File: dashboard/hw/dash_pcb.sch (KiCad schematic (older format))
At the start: 3 parts, among them J1 LCD, J2 DEBUG, U1 LPC11C24FBD48

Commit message: update connectors for the lcd actually used
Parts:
- added J3: LCD_BL, Connectors_JST:JST_XH_S03B-XH-A_03x2.50mm_Angled, symbol Conn_01x03
- added RV1: 10k, Potentiometers:Potentiometer_Trimmer_ACP_CA6v_Horizontal, symbol POT
- J1: footprint Socket_Strips:Socket_Strip_Straight_2x11_Pitch2.54mm -> Socket_Strips:Socket_Strip_Straight_2x10_Pitch2.54mm; symbol Conn_02x11_Odd_Even -> Conn_02x10_Odd_Even
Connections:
- wire segments 22 -> 25
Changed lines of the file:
@@
 $EndComp
 $Comp
-L Conn_02x11_Odd_Even J1
+L Conn_02x10_Odd_Even J1
 U 1 1 5ADCA11A
-P 9200 3300
-F 0 "J1" H 9250 3900 50  0000 C CNN
-F 1 "LCD" H 9250 2700 50  0000 C CNN
-F 2 "Socket_Strips:Socket_Strip_Straight_2x11_Pitch2.54mm" H 9200 3300 50  0001 C CNN
-F 3 "" H 9200 3300 50  0001 C CNN
-	1    9200 3300
-	1    0    0    -1
-$EndComp
-$Comp
-L GND #PWR7
+P 9200 3200
+F 0 "J1" H 9250 3700 50  0000 C CNN
+F 1 "LCD" H 9250 2600 50  0000 C CNN
+F 2 "Socket_Strips:Socket_Strip_Straight_2x10_Pitch2.54mm" H 9200 3200 50  0001 C CNN
+F 3 "" H 9200 3200 50  0001 C CNN
+	1    9200 3200
+	1    0    0    -1
+$EndComp
+$Comp
+L GND #PWR9
 U 1 1 5ADCA1A0
 P 9250 2600
-F 0 "#PWR7" H 9250 2350 50  0001 C CNN
+F 0 "#PWR9" H 9250 2350 50  0001 C CNN
 F 1 "GND" H 9250 2450 50  0000 C CNN
 F 2 "" H 9250 2600 50  0001 C CNN
@@
 Text Label 9000 3700 2    60   ~ 0
 LCD_FS
-Text Label 9500 3700 0    60   ~ 0
+Text Label 9000 3200 2    60   ~ 0
 LCD_VEE
-Text Label 9000 3800 2    60   ~ 0
-LCD_LED_A
-Text Label 9500 3800 0    60   ~ 0
-LCD_LED_K
 $Comp
 L GND #PWR2
@@
 Text Label 4400 3100 2    60   ~ 0
 LCD_DB1
-Text Label 4400 3200 2    60   ~ 0
+Text Label 4400 4800 2    60   ~ 0
 LCD_DB2
-Text Label 4400 3300 2    60   ~ 0
+Text Label 4400 4500 2    60   ~ 0
 LCD_DB3
 Text Label 4400 3400 2    60   ~ 0
@@
 $EndComp
 $Comp
-L +3V3 #PWR9
+L +3V3 #PWR11
 U 1 1 5ADCAB0C
 P 9500 5800
-F 0 "#PWR9" H 9500 5650 50  0001 C CNN
+F 0 "#PWR11" H 9500 5650 50  0001 C CNN
 F 1 "+3V3" H 9500 5940 50  0000 C CNN
 F 2 "" H 9500 5800 50  0001 C CNN
@@
 	9500 5800 9500 5900
 $Comp
-L GND #PWR8
+L GND #PWR10
 U 1 1 5ADCAB42
 P 9350 6300
-F 0 "#PWR8" H 9350 6050 50  0001 C CNN
+F 0 "#PWR10" H 9350 6050 50  0001 C CNN
 F 1 "GND" H 9350 6150 50  0000 C CNN
 F 2 "" H 9350 6300 50  0001 C CNN
@@
 Text Label 6800 2900 0    60   ~ 0
 LCD_C/~D
-Text Label 6800 3400 0    60   ~ 0
-LCD_~CE
 Text Label 6800 3300 0    60   ~ 0
 LCD_~RST
-Text Label 6800 4000 0    60   ~ 0
-LCD_FS
 Text Label 6800 3200 0    60   ~ 0
 LCD_~WR
@@
 CANL
 $Comp
-L +3V3 #PWR?
+L +3V3 #PWR8
 U 1 1 5AE5BC1B
 P 8800 2600
-F 0 "#PWR?" H 8800 2450 50  0001 C CNN
+F 0 "#PWR8" H 8800 2450 50  0001 C CNN
 F 1 "+3V3" H 8800 2740 50  0000 C CNN
 F 2 "" H 8800 2600 50  0001 C CNN
@@
 	1    0    0    -1
 $EndComp
+$Comp
+L +3V3 #PWR7
+U 1 1 5AE5BE05
+P 8450 3700
+F 0 "#PWR7" H 8450 3550 50  0001 C CNN
+F 1 "+3V3" H 8450 3840 50  0000 C CNN
+F 2 "" H 8450 3700 50  0001 C CNN
+F 3 "" H 8450 3700 50  0001 C CNN
+	1    8450 3700
+	1    0    0    -1
+$EndComp
+Wire Wire Line
+	8450 3700 9000 3700
+$Comp
+L GND #PWR6
+U 1 1 5AE5BE6A
+P 8450 3100
+F 0 "#PWR6" H 8450 2850 50  0001 C CNN
+F 1 "GND" H 8450 2950 50  0000 C CNN
+F 2 "" H 8450 3100 50  0001 C CNN
+F 3 "" H 8450 3100 50  0001 C CNN
+	1    8450 3100
+	1    0    0    -1
+$EndComp
+Wire Wire Line
+	8450 3100 9000 3100
+Text Label 10650 3500 2    60   ~ 0
+LCD_LED_A
+Text Label 10650 3700 2    60   ~ 0
+LCD_LED_K
+$Comp
+L Conn_01x03 J3
+U 1 1 5AE5C0EF
+P 10850 3600
+F 0 "J3" H 10850 3800 50  0000 C CNN
+F 1 "LCD_BL" H 10850 3400 50  0000 C CNN
+F 2 "Connectors_JST:JST_XH_S03B-XH-A_03x2.50mm_Angled" H 10850 3600 50  0001 C CNN
+F 3 "" H 10850 3600 50  0001 C CNN
+	1    10850 3600
+	1    0    0    -1
+$EndComp
+$Comp
+L POT RV1
+U 1 1 5AE5C369
+P 10550 2800
+F 0 "RV1" V 10375 2800 50  0000 C CNN
+F 1 "10k" V 10450 2800 50  0000 C CNN
+F 2 "Potentiometers:Potentiometer_Trimmer_ACP_CA6v_Horizontal" H 10550 2800 50  0001 C CNN
+F 3 "" H 10550 2800 50  0001 C CNN
+	1    10550 2800
+	0    -1   -1   0
+$EndComp
+$Comp
+L GND #PWR12
+U 1 1 5AE5C42C
+P 10850 2800
+F 0 "#PWR12" H 10850 2550 50  0001 C CNN
+F 1 "GND" H 10850 2650 50  0000 C CNN
+F 2 "" H 10850 2800 50  0001 C CNN
+F 3 "" H 10850 2800 50  0001 C CNN
+	1    10850 2800
+	1    0    0    -1
+$EndComp
+Wire Wire Line
+	10700 2800 10850 2800
+Text Label 10550 2650 0    60   ~ 0
+LCD_V0
+Text Label 10400 2800 2    60   ~ 0
+LCD_VEE
 $EndSCHEMATC

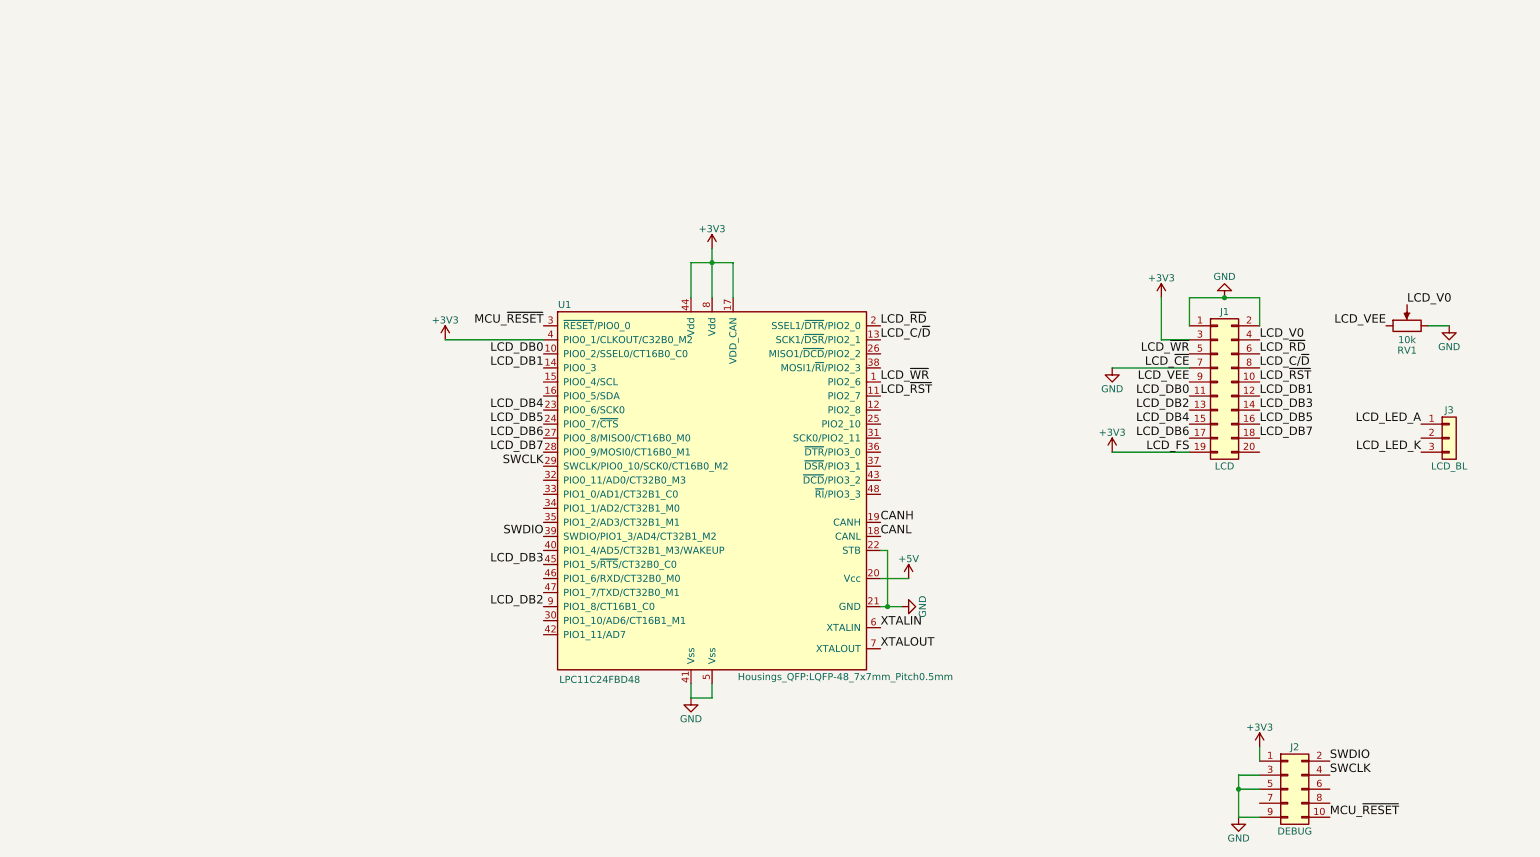
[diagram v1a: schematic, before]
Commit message: add misc passives to dash pcb
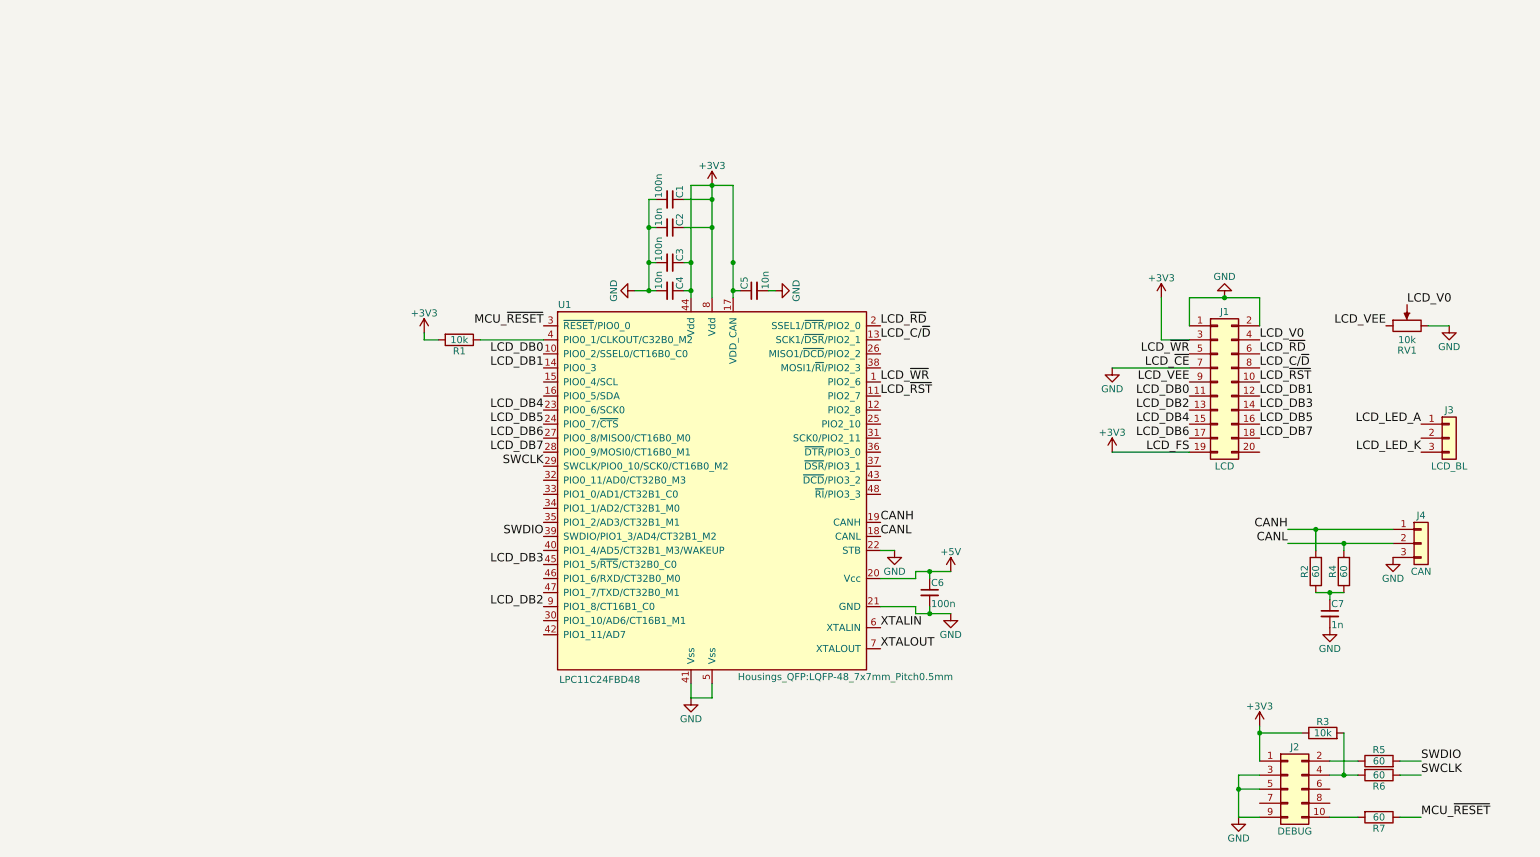
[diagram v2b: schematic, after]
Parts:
- added C1, C3, C6: 100n, Capacitors_SMD:C_0603, symbol C_Small
- added C2, C4, C5: 10n, Capacitors_SMD:C_0603, symbol C_Small
- added C7: 1n, Capacitors_SMD:C_0603, symbol C_Small
- added J4: CAN, Pin_Headers:Pin_Header_Angled_1x03_Pitch2.54mm, symbol Conn_01x03
- added R1, R3: 10k, Resistors_SMD:R_0603, symbol R
- added R2, R4, R5, R6, R7: 60, Resistors_SMD:R_0603, symbol R
- J2: footprint Pin_Headers:Pin_Header_Straight_2x05_Pitch1.27mm -> Pin_Headers:Pin_Header_Angled_2x05_Pitch1.27mm
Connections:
- net +3V3: now also C1.1, C2.1, C3.1, C4.1, C5.1, R1.2, R3.1; no longer U1.4 (PIO0_1/CLKOUT/C32B0_M2)
- net +5V: now also C6.1
- net CANH: now also J4.1 (Pin_1), R2.2
- net CANL: now also J4.2 (Pin_2), R4.2
- net GND: now also C1.2, C2.2, C3.2, C4.2, C5.2, C6.2, C7.2, J4.3 (Pin_3)
- net MCU_~RESET: now also R7.1; no longer J2.10 (Pin_10)
- net SWCLK: now also R6.1; no longer J2.4 (Pin_4)
- net SWDIO: now also R5.2; no longer J2.2 (Pin_2)
- new net: R1.1, U1.4 (PIO0_1/CLKOUT/C32B0_M2)
- new net: J2.10 (Pin_10), R7.2
- new net: J2.2 (Pin_2), R5.1
- new net: J2.4 (Pin_4), R3.2, R6.2
- new net: C7.1, R2.1, R4.1

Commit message: add schematic symbol for lmz21700 power module
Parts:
- added U?: LMZ21700, symbol LMZ21700
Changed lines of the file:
@@
 LIBS:valves
 LIBS:nxp_can
+LIBS:lmz21700
 LIBS:dash_pcb-cache
 EELAYER 25 0
@@
 Wire Wire Line
 	3550 2900 3650 2900
+$Comp
+L LMZ21700 U?
+U 1 1 5AEFF749
+P 1850 1450
+F 0 "U?" H 1600 850 60  0000 C CNN
+F 1 "LMZ21700" H 1850 1450 60  0000 C CNN
+F 2 "" H 2200 1300 60  0001 C CNN
+F 3 "" H 2200 1300 60  0001 C CNN
+	1    1850 1450
+	1    0    0    -1
+$EndComp
 $EndSCHEMATC

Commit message: add tps62175 which we are actually using
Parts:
- removed U?: LMZ21700, symbol LMZ21700
- added U?: TPS62175, symbol TPS62175
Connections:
- net labels added: 5VPG
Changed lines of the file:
@@
 LIBS:nxp_can
 LIBS:lmz21700
+LIBS:tps6217x
 LIBS:dash_pcb-cache
 EELAYER 25 0
@@
 Wire Wire Line
 	3550 2900 3650 2900
-$Comp
-L LMZ21700 U?
-U 1 1 5AEFF749
-P 1850 1450
-F 0 "U?" H 1600 850 60  0000 C CNN
-F 1 "LMZ21700" H 1850 1450 60  0000 C CNN
-F 2 "" H 2200 1300 60  0001 C CNN
-F 3 "" H 2200 1300 60  0001 C CNN
-	1    1850 1450
-	1    0    0    -1
-$EndComp
+Text Label 2800 1700 0    60   ~ 0
+5VPG
+$Comp
+L TPS62175 U?
+U 1 1 5AF00B83
+P 2300 1350
+F 0 "U?" H 2050 850 60  0000 C CNN
+F 1 "TPS62175" H 2300 1300 60  0000 C CNN
+F 2 "" H 2300 1400 60  0001 C CNN
+F 3 "" H 2300 1400 60  0001 C CNN
+	1    2300 1350
+	1    0    0    -1
+$EndComp

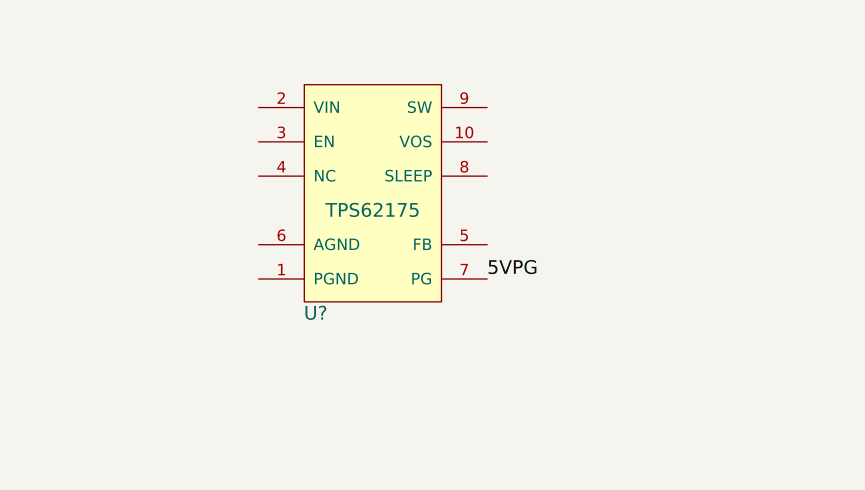
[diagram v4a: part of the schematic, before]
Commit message: wire up the 5v converter
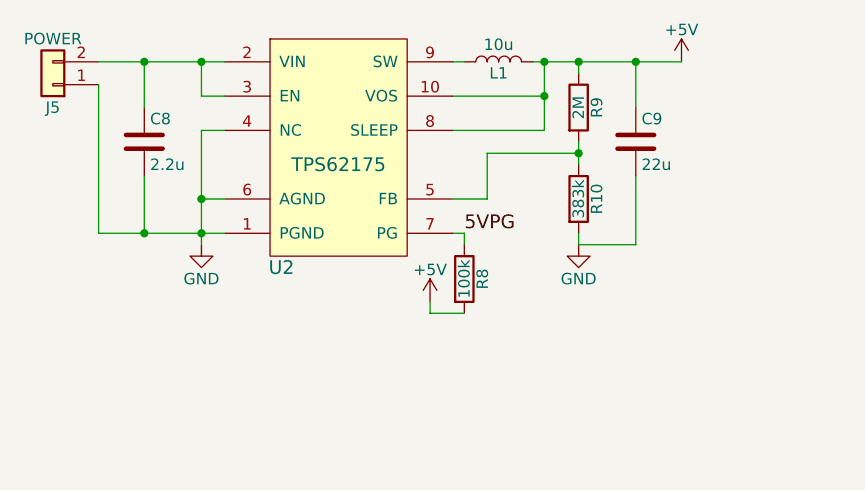
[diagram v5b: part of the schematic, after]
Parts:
- added C8: 2.2u, Capacitors_SMD:C_0603, symbol C
- added C9: 22u, Capacitors_SMD:C_0603, symbol C
- added J5: POWER, Pin_Headers:Pin_Header_Angled_1x02_Pitch2.00mm, symbol Conn_01x02
- added L1: 10u, symbol L
- added R10: 383k, Resistors_SMD:R_0603, symbol R
- added R8: 100k, Resistors_SMD:R_0603, symbol R
- added R9: 2M, Resistors_SMD:R_0603, symbol R
- gave numbers to parts that had none: 1
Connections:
- net +5V: now also U2.10 (VOS), U2.8 (SLEEP), C9.1, L1.2, R8.2, R9.1
- net 5VPG: now also R8.1
- net GND: now also U2.1 (PGND), U2.4 (NC), U2.6 (AGND), C8.2, C9.2, J5.1 (Pin_1), R10.2
- net at U2.2 (VIN): now also U2.3 (EN), C8.1, J5.2 (Pin_2)
- net at U2.5 (FB): now also R10.1, R9.2
- net at U2.9 (SW): now also L1.1
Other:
- moved on the sheet: U2
